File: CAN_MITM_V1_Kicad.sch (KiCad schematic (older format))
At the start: 7 parts, among them IC2 SN65HVD234, IC3 SN65HVD234

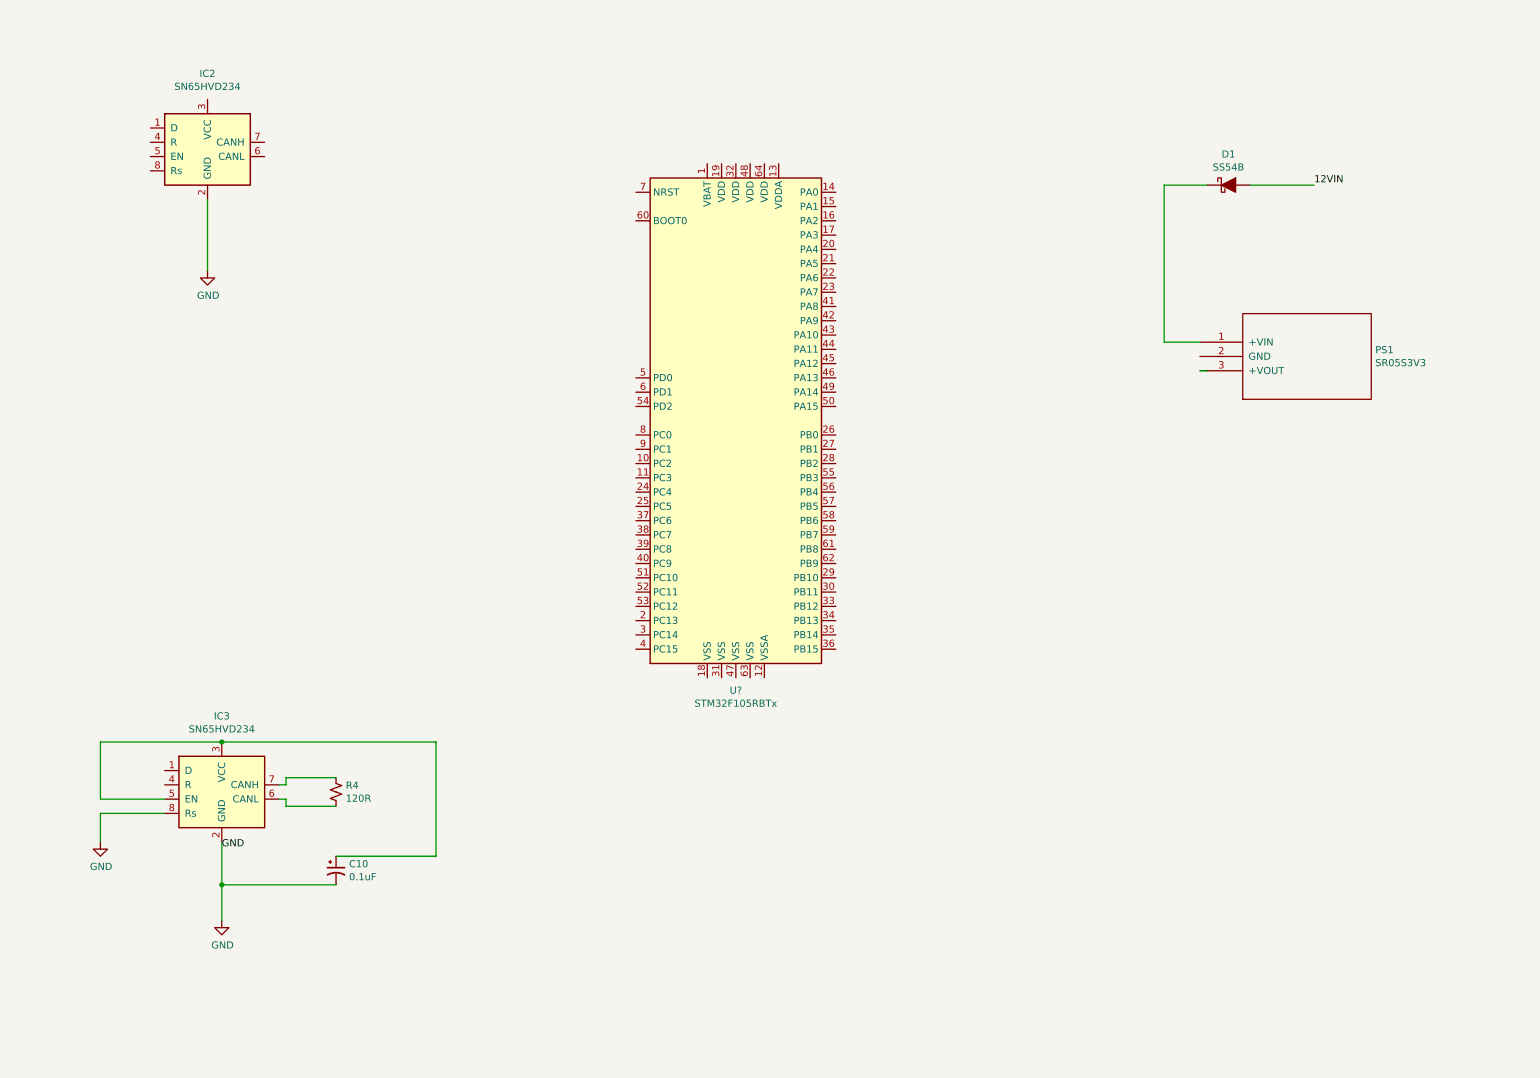
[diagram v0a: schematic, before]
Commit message: Adding more to the Kicad schematic
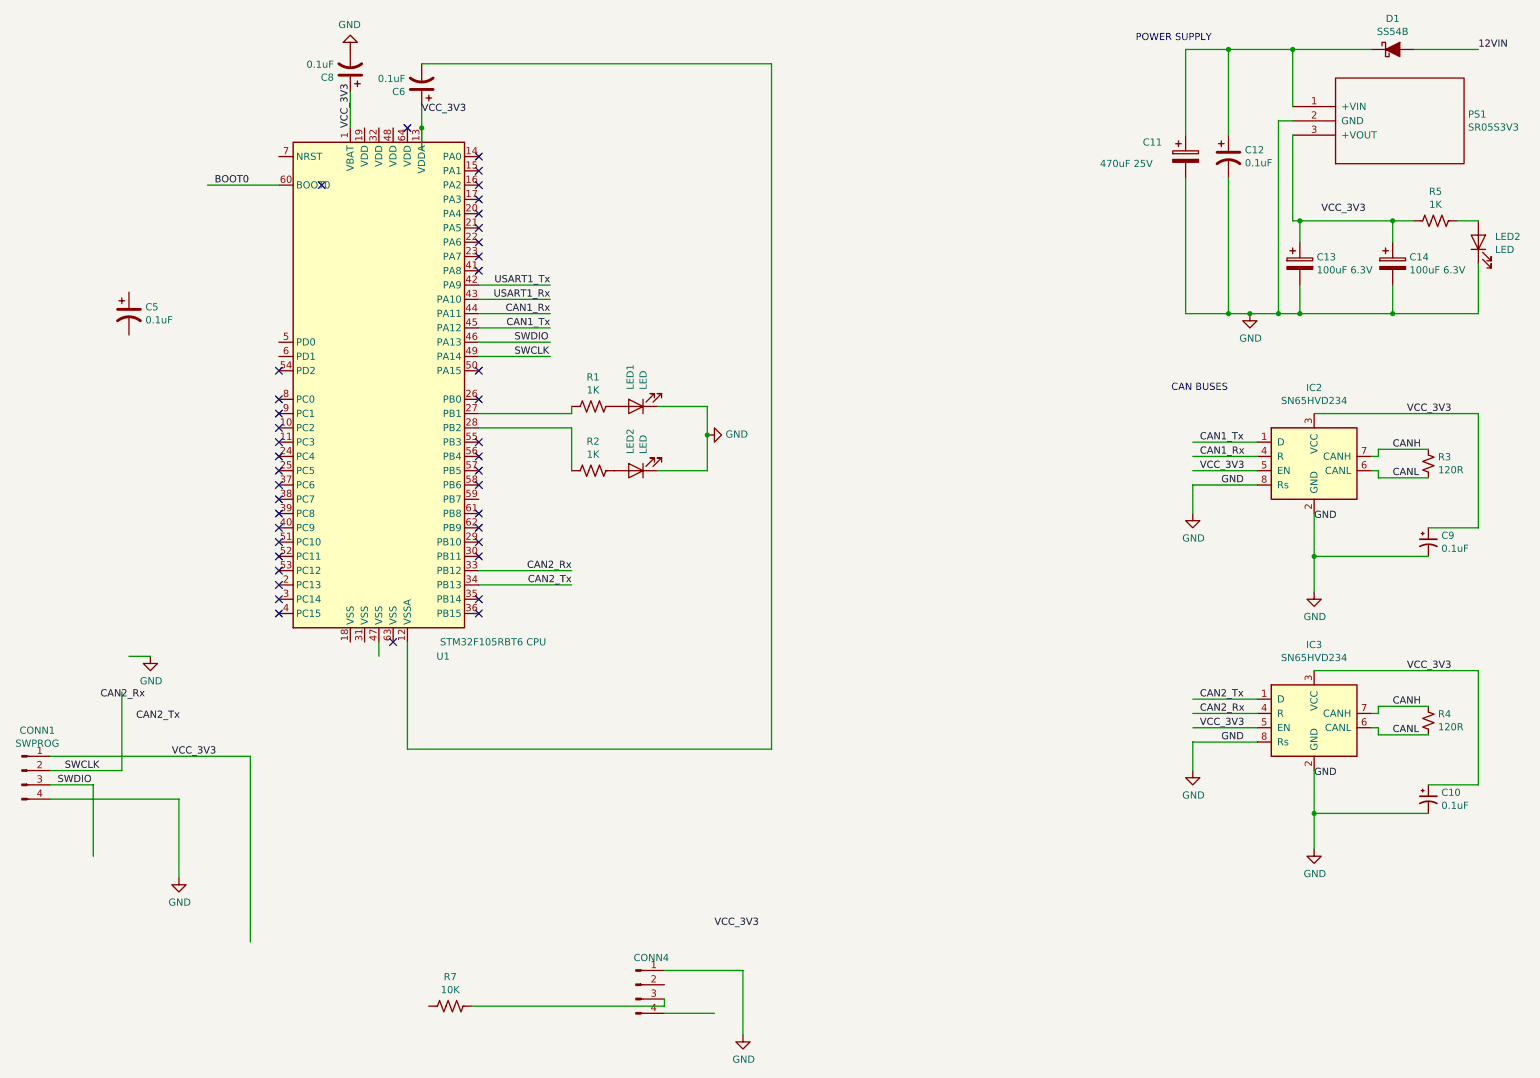
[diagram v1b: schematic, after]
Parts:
- added C11: 470uF 25V, Capacitor_SMD:C_0805_2012Metric, symbol Device:CP
- added C12, C5, C6, C8: 0.1uF, Capacitor_SMD:C_0805_2012Metric, symbol Device:CP1
- added C13, C14: 100uF 6.3V, Capacitor_SMD:C_0805_2012Metric, symbol Device:CP
- added C9: 0.1uF, Capacitor_SMD:C_0805_2012Metric, symbol Device:CP1_Small
- added CONN1: SWPROG, TerminalBlock_TE-Connectivity:TerminalBlock_TE_282834-4_1x04_P2.54mm_Horizontal, symbol Connector:Conn_01x04_Male
- added CONN4: Conn_01x04_Male, TerminalBlock_TE-Connectivity:TerminalBlock_TE_282834-4_1x04_P2.54mm_Horizontal, symbol Connector:Conn_01x04_Male
- added LED1, LED2 (x2): LED, LED_SMD:LED_0805_2012Metric, symbol Device:LED
- added R1, R2, R5: 1K, Resistor_SMD:R_0805_2012Metric, symbol Device:R_US
- added R3: 120R, Resistor_SMD:R_0805_2012Metric, symbol Device:R_Small_US
- added R7: 10K, Resistor_SMD:R_0805_2012Metric, symbol Device:R_US
- C10: footprint (none) -> Capacitor_SMD:C_0805_2012Metric
- D1: footprint (none) -> Diode_SMD:D_SMA
- PS1: footprint MODULE -> Converter_DCDC:SR05S3V3
- R4: footprint (none) -> Resistor_SMD:R_0805_2012Metric
- U1: renamed from U?; value STM32F105RBTx -> STM32F105RBT6 CPU
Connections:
- net labels added: BOOT0, CAN1_Rx, CAN1_Tx, CAN2_Rx, CAN2_Tx, CANH, CANL, SWCLK, SWDIO, USART1_Rx, USART1_Tx, VCC_3V3
- wire segments 23 -> 100
- no-connect marks 0 -> 41
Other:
- note added: "CAN BUSES"
- note added: "POWER SUPPLY"
- moved on the sheet: D1, PS1, U1
